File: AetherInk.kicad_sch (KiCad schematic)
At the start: 0 parts

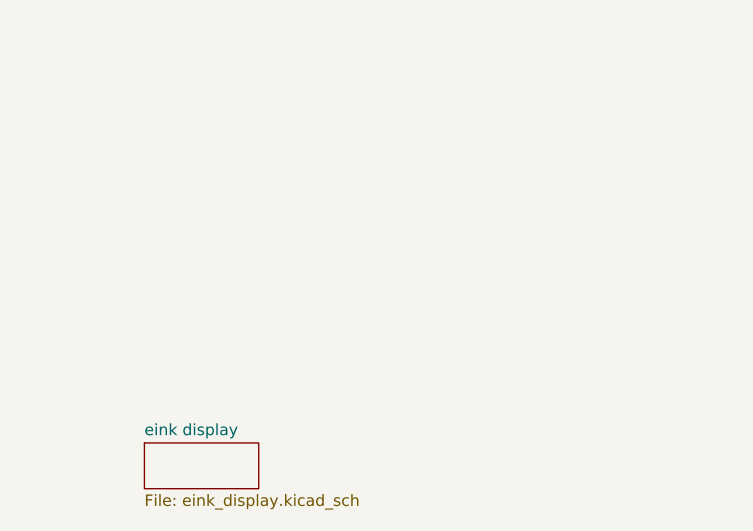
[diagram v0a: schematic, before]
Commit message: done the power sch for the mcu
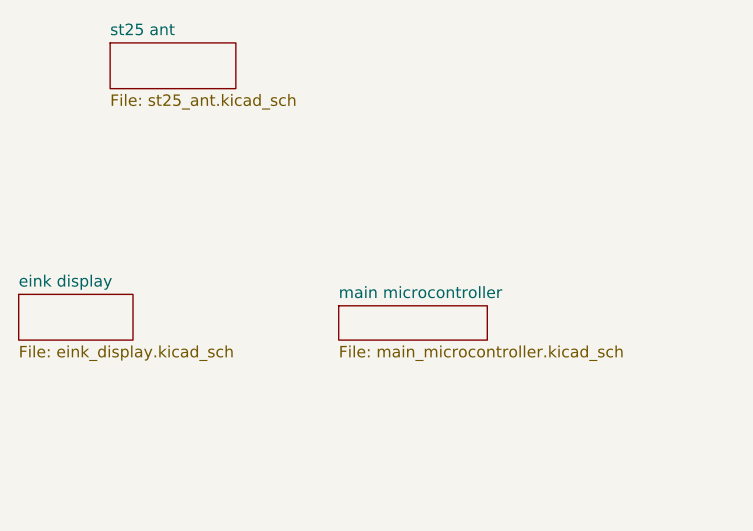
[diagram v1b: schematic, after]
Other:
- added sheet main microcontroller (main_microcontroller.kicad_sch)
- added sheet st25 ant (st25_ant.kicad_sch)
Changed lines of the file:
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@@
 	(paper "A4")
 	(sheet
-		(at 130.81 101.6)
+		(at 116.84 85.09)
 		(size 12.7 5.08)
 		(exclude_from_sim no)
@@
 		)
 		(property "Sheetname" "eink display"
-			(at 130.81 100.8884 0)
+			(at 116.84 84.3784 0)
 			(show_name no)
 			(do_not_autoplace no)
@@
 		)
 		(property "Sheetfile" "eink_display.kicad_sch"
-			(at 130.81 107.2646 0)
+			(at 116.84 90.7546 0)
 			(show_name no)
 			(do_not_autoplace no)
@@
 				)
 			)
+		)
+	)
+	(sheet
+		(at 127 57.15)
+		(size 13.97 5.08)
+		(exclude_from_sim no)
+		(in_bom yes)
+		(on_board yes)
+		(dnp no)
+		(fields_autoplaced yes)
+		(stroke
+			(width 0.1524)
+			(type solid)
+		)
+		(fill
+			(color 0 0 0 0)
+		)
+		(property "Sheetname" "st25 ant"
+			(at 127 56.4384 0)
+			(show_name no)
+			(do_not_autoplace no)
+			(effects
+				(font
+					(size 1.27 1.27)
+				)
+				(justify left bottom)
+			)
+		)
+		(property "Sheetfile" "st25_ant.kicad_sch"
+			(at 127 62.8146 0)
+			(show_name no)
+			(do_not_autoplace no)
+			(effects
+				(font
+					(size 1.27 1.27)
+				)
+				(justify left top)
+			)
+		)
+		(instances
+			(project "AetherInk"
+				(path "/bfe982fc-ac83-4361-b0ed-d42b62c23a78"
+					(page "4")
+				)
+			)
+		)
+	)
+	(sheet
+		(at 152.4 86.36)
+		(size 16.51 3.81)
+		(exclude_from_sim no)
+		(in_bom yes)
+		(on_board yes)
+		(dnp no)
+		(fields_autoplaced yes)
+		(stroke
+			(width 0.1524)
+			(type solid)
+		)
+		(fill
+			(color 0 0 0 0)
+		)
+		(property "Sheetname" "main microcontroller"
+			(at 152.4 85.6484 0)
+			(show_name no)
+			(do_not_autoplace no)
+			(effects
+				(font
+					(size 1.27 1.27)
+				)
+				(justify left bottom)
+			)
+		)
+		(property "Sheetfile" "main_microcontroller.kicad_sch"
+			(at 152.4 90.7546 0)
+			(show_name no)
+			(do_not_autoplace no)
+			(effects
+				(font
+					(size 1.27 1.27)
+				)
+				(justify left top)
+			)
+		)
+		(instances
+			(project "AetherInk"
+				(path "/bfe982fc-ac83-4361-b0ed-d42b62c23a78"
+					(page "3")
+				)
+			)
